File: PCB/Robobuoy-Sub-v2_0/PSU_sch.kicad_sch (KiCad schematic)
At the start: 69 parts, among them J201 Accu 1, J202 LoadbalanceAccu1, J203 LoadbalanceAccu2, J204 CHARGE/ON-OFF, J205 Accu 2, J206 ESCSB, J207 ESCBB, Q201 AO3400A, Q202 AO3400A, Q203 AO3400A, Q204 AO3400A, Q205 AO3400A, Q206 AO3400A, Q207 AO3400A, Q208 AO3400A, SW201 On/Off, U201 TPS5430DDAR, U202 SN74LV1T34DBV, U203 SN74LV1T34DBV, U204 TLV61046ADB

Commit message: Pc programm starting to code
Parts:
- removed C216: 100n, A_Device:C_0603, symbol Device:C_Small
- removed Q203, Q205, Q207: AO3400A, Package_TO_SOT_SMD:SOT-23, symbol Transistor_FET:2N7002
- removed R208: 1.8k, A_Device:R_0603, symbol Device:R_Small
- removed U202: SN74LV1T34DBV, Package_TO_SOT_SMD:SOT-23-5, symbol Logic_LevelTranslator:SN74LV1T34DBV
- added Q203, Q205, Q207, Q209: AO3401A, Package_TO_SOT_SMD:SOT-23, symbol Transistor_FET:AO3401A
- added R208, R214, R215: 10K, A_Device:R_0603, symbol Device:R
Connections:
- net GND: now also J206.1 (Pin_1), R208.1
- net PWR_ESC_SB: now also R209.2
- net Vbatt: now also Q203.2 (S), Q205.2 (S), Q207.2 (S), Q209.2 (S), R215.1; no longer J206.2 (Pin_2)
- net at Q201.1 (G), R209.1: no longer TP207.1
- net at D205.2 (A): now also J206.2 (Pin_2), Q203.3 (D), Q205.3 (D), Q207.3 (D), Q209.3 (D)
- new net: Q201.3 (D), R214.1
- new net: D205.1 (K), R208.2
- new net: Q203.1 (G), Q205.1 (G), Q207.1 (G), Q209.1 (G), R214.2, R215.2, TP207.1
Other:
- moved on the sheet: D205, J206, TP207

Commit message: Many changes again :)
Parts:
- removed C209, C210, C215, C217, C219: 100n, A_Device:C_0603, symbol Device:C_Small
- removed C218: 4.7uF/10V, A_Device:C_1206_(1.6), symbol Device:C_Small
- removed D206: ESC_SB, A_Passive:LED_0805, symbol Device:LED_Small
- removed D6: 5V, A_Passive:LED_0805, symbol Device:LED_Small
- removed J202: LoadbalanceAccu1, Connector_JST:JST_XH_B7B-XH-A_1x07_P2.50mm_Vertical, symbol Connector:Conn_01x07_Pin
- removed J203: LoadbalanceAccu2, Connector_JST:JST_XH_B7B-XH-A_1x07_P2.50mm_Vertical, symbol Connector:Conn_01x07_Pin
- removed J204: CHARGE/ON-OFF, A_Connector:T4140012121000, symbol Connector:Conn_01x12_Socket
- removed L202: 10uH, A_Device:FTC252012S, symbol Device:L_Small
- removed Q204, Q206, Q208: AO3400A, Package_TO_SOT_SMD:SOT-23, symbol Transistor_FET:2N7002
- removed R19, R210: 1.8k, A_Device:R_0603, symbol Device:R_Small
- removed R20: 1k, A_Device:R_0603, symbol Device:R_Small
- removed R211: 100, A_Device:R_0603, symbol Device:R_Small
- removed R212: 82K, A_Device:R_0603, symbol Device:R_Small
- removed R213: 15K, A_Device:R_0603, symbol Device:R_Small
- removed TP208: ESC_BB-POWER-5V, A_Pads_Pins:Testpad_1, symbol Connector:TestPoint_Small
- removed TP209: 0.795V, A_Pads_Pins:Testpad_1, symbol Connector:TestPoint_Small
- removed TP210: 5V, A_Pads_Pins:Testpad_1, symbol Connector:TestPoint_Small
- removed U203: SN74LV1T34DBV, Package_TO_SOT_SMD:SOT-23-5, symbol Logic_LevelTranslator:SN74LV1T34DBV
- removed U204: TLV61046ADB, Package_TO_SOT_SMD:SOT-23-6, symbol Regulator_Switching:TLV61046ADB
- added D203: ESC_BB, A_Passive:LED_0805, symbol Device:LED_Small
- added Q204, Q206, Q208, Q210: AO3401A, Package_TO_SOT_SMD:SOT-23, symbol Transistor_FET:AO3401A
- added R206: 10K, A_Device:R_0603, symbol Device:R_Small
- added R207: 100, A_Device:R_0603, symbol Device:R_Small
- added R210, R211, R212: 10K, A_Device:R_0603, symbol Device:R
- added TP205: ESC_SB-POWER-5V, A_Pads_Pins:Testpad_1, symbol Connector:TestPoint_Small
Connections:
- net +3.3V: now also R206.2
- net GND: now also J207.1 (Pin_1), R212.1
- net PWR_ESC_BB: now also R207.2
- net Vbatt: now also Q204.2 (S), Q206.2 (S), Q208.2 (S), Q210.2 (S), R211.1; no longer J207.2 (Pin_2)
- net at Q202.1 (G): now also R207.1
- net at Q202.3 (D): now also R210.1; no longer J207.1 (Pin_1)
- net at D7.2 (A): now also R206.1
- new net: D203.2 (A), J207.2 (Pin_2), Q204.3 (D), Q206.3 (D), Q208.3 (D), Q210.3 (D)
- new net: D203.1 (K), R212.2
- new net: Q204.1 (G), Q206.1 (G), Q208.1 (G), Q210.1 (G), R210.2, R211.2, TP205.1
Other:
- moved on the sheet: D205, D7, J206, J207, Q201, Q203, Q205, Q207, Q209, R208, R209, R214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

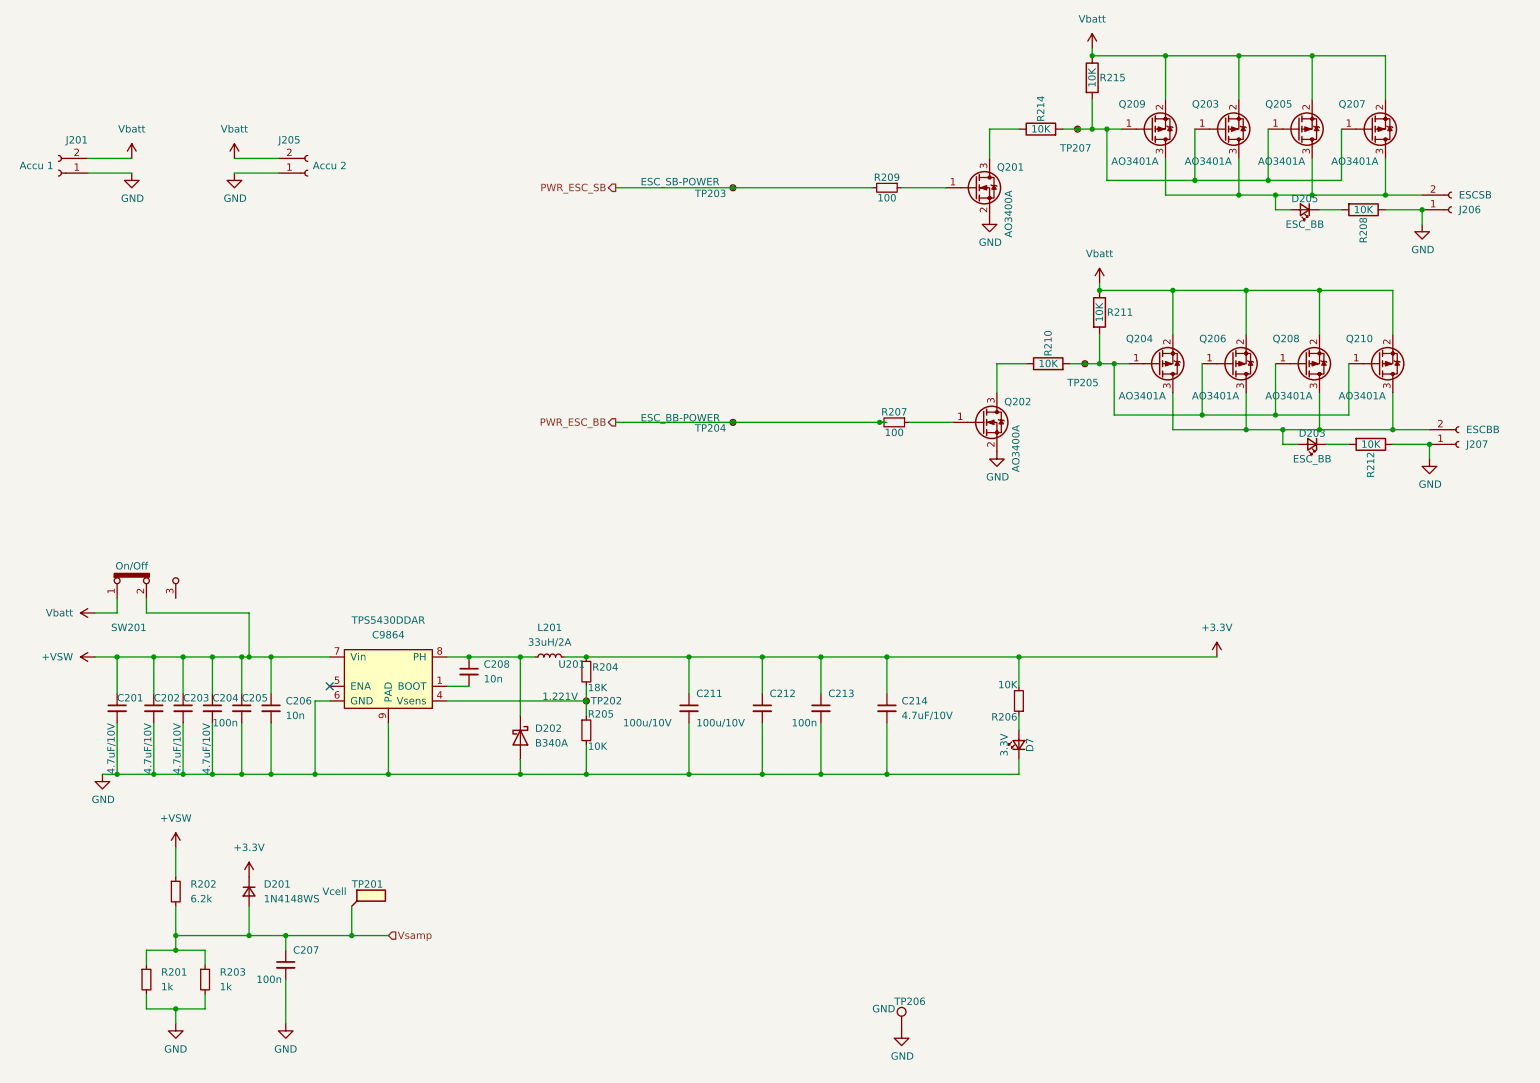
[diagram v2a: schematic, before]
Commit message: Struct re defined. not finished yet
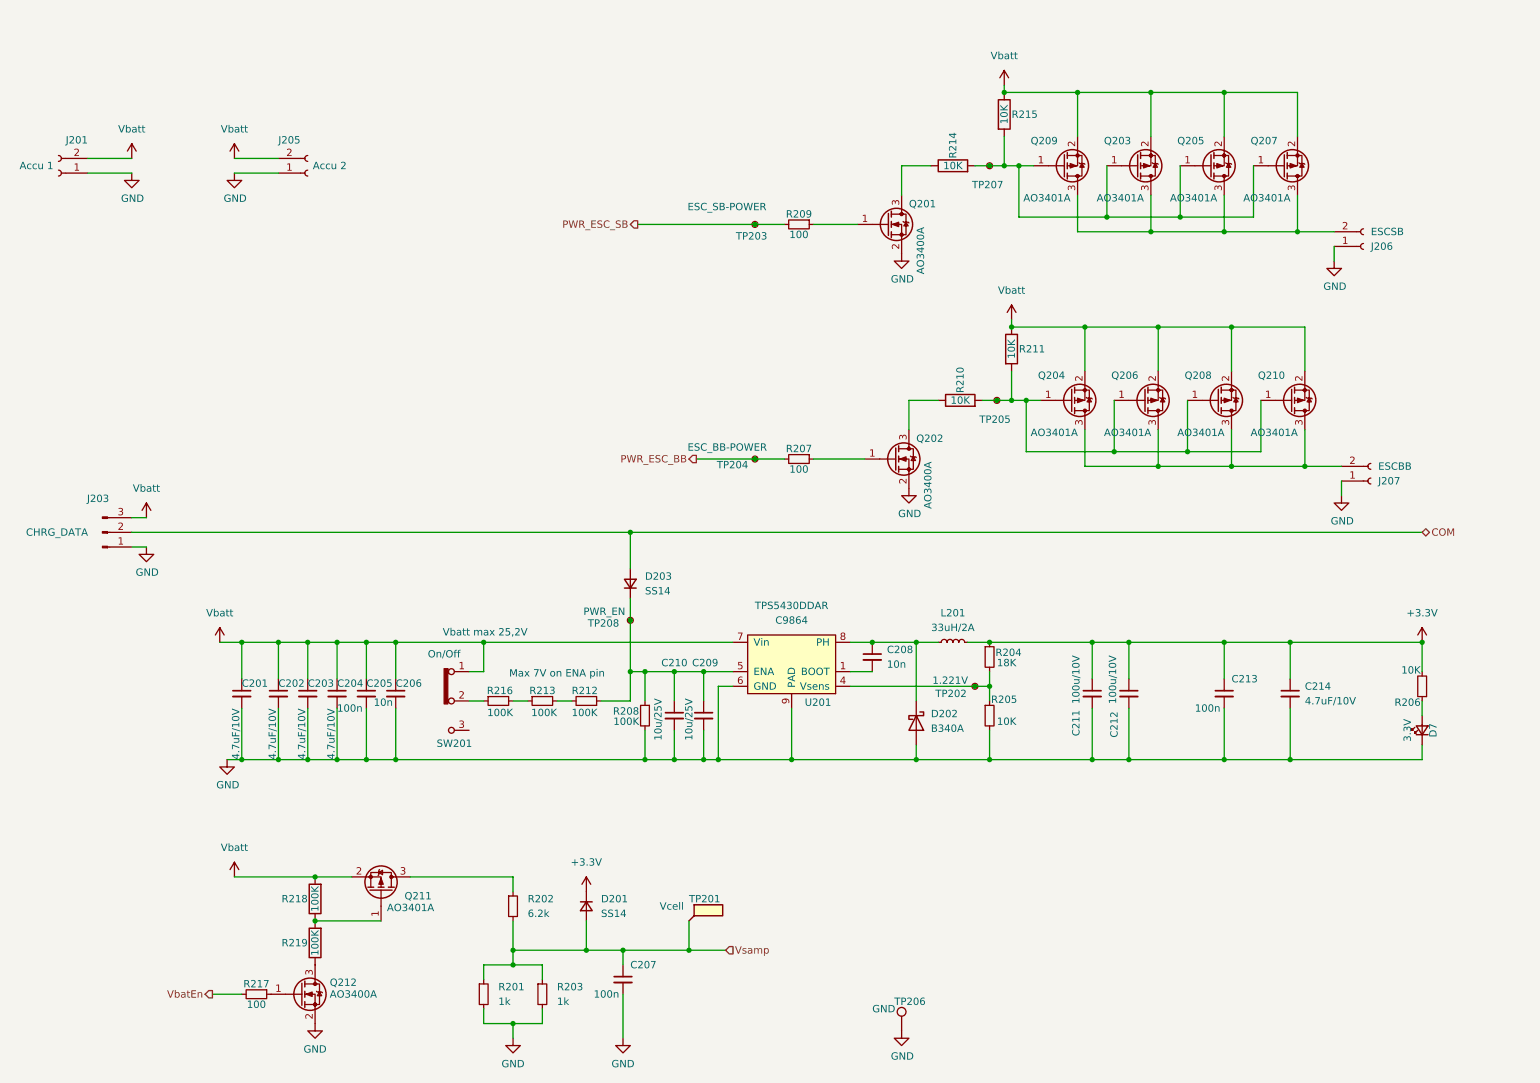
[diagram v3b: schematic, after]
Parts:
- removed D203, D205: ESC_BB, A_Passive:LED_0805, symbol Device:LED_Small
- removed R208, R212: 10K, A_Device:R_0603, symbol Device:R
- added C209, C210: 10u/25V, A_Device:C_0805, symbol Device:C_Small
- added D203: SS14, A_Device:D_SMA_4.3x3x2.4, symbol Device:D_Small
- added J203: CHRG_DATA, Connector_JST:JST_XH_B3B-XH-A_1x03_P2.50mm_Vertical, symbol Connector:Conn_01x03_Pin
- added Q211: AO3401A, Package_TO_SOT_SMD:SOT-23, symbol Transistor_FET:AO3401A
- added Q212: AO3400A, Package_TO_SOT_SMD:SOT-23, symbol Transistor_FET:2N7002
- added R208, R212, R213, R216: 100K, A_Device:R_0603, symbol Device:R_Small
- added R217: 100, A_Device:R_0603, symbol Device:R_Small
- added R218, R219: 100K, A_Device:R_0603, symbol Device:R
- added TP208: PWR_EN, A_Pads_Pins:Testpad_1, symbol Connector:TestPoint_Small
- D201: value 1N4148WS -> SS14; footprint A_Device:D_SOD-323_1.8x1.4x1.15 -> A_Device:D_SMA_4.3x3x2.4; LCSC C2128 -> C2480
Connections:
- net GND: now also C209.2, C210.2, J203.1 (Pin_1), Q212.2 (S), R208.2
- net Vbatt: now also C201.1, C202.1, C203.1, C204.1, C205.1, C206.1, U201.7 (Vin), J203.3 (Pin_3), Q211.2 (S), R218.2
- net at U201.5 (ENA): now also C209.1, C210.1, D203.1 (K), R208.1, R212.1, TP208.1
- removed net +VSW: C201.1, C202.1, C203.1, C204.1, C205.1, C206.1, R202.1, SW201.2, U201.7 (Vin)
- new net: Q212.1 (G), R217.1
- new net: Q212.3 (D), R219.1
- new net: R216.1, SW201.2
- new net: R213.1, R216.2
- new net: Q211.3 (D), R202.1
- new net: R212.2, R213.2
- new net: Q211.1 (G), R218.1, R219.2
- new net COM: D203.2 (A), J203.2 (Pin_2)
- new net VbatEn: R217.2
- no-connect marks 1 -> 0
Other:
- note added: "Max 7V on ENA pin"
- note added: "Vbatt max 25,2V"
- moved on the sheet: C201, C202, C203, C204, C205, C206, C207, C208, C211, C212, C213, C214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

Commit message: Many changes
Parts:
- removed J201: Accu 1, A_Connector:AMASS_XT60-M_1x02_P7.20mm_Vertical, symbol Connector:Conn_01x02_Socket
- removed J203: CHRG_DATA, Connector_JST:JST_XH_B3B-XH-A_1x03_P2.50mm_Vertical, symbol Connector:Conn_01x03_Pin
- removed J205: Accu 2, A_Connector:AMASS_XT60-M_1x02_P7.20mm_Vertical, symbol Connector:Conn_01x02_Socket
- removed J206: ESCSB, A_Connector:AMASS_XT60-F_1x02_P7.20mm_Vertical, symbol Connector:Conn_01x02_Socket
- removed J207: ESCBB, A_Connector:AMASS_XT60-F_1x02_P7.20mm_Vertical, symbol Connector:Conn_01x02_Socket
- removed Q201, Q202: AO3400A, Package_TO_SOT_SMD:SOT-23, symbol Transistor_FET:2N7002
- removed Q203, Q204, Q205, Q206, Q207, Q208, Q209, Q210: AO3401A, Package_TO_SOT_SMD:SOT-23, symbol Transistor_FET:AO3401A
- removed R207, R209: 100, A_Device:R_0603, symbol Device:R_Small
- removed R210, R211, R214, R215: 10K, A_Device:R_0603, symbol Device:R
- removed TP203: ESC_SB-POWER, A_Pads_Pins:Testpad_1, symbol Connector:TestPoint_Small
- removed TP204: ESC_BB-POWER, A_Pads_Pins:Testpad_1, symbol Connector:TestPoint_Small
- removed TP205, TP207: ESC_SB-POWER-5V, A_Pads_Pins:Testpad_1, symbol Connector:TestPoint_Small
- added D201: SS14, A_Device:D_SMA_4.3x3x2.4, symbol Device:D_Small
- added J202: CHRG/DATA, Connector_Wire:SolderWire-0.75sqmm_1x03_P4.8mm_D1.25mm_OD2.3mm, symbol Connector:Conn_01x03_Pin
- D204: renamed from D202; value B340A -> SS54; LCSC C85098 -> C22452
- renumbered C210 to C208, C208 to C210, D201 to D202, Q212 to Q201, Q211 to Q202, R217 to R201, R218 to R202, R219 to R203, R201 to R204, R216 to R205, R202 to R206, R213 to R207, R203 to R208, R212 to R209, R208 to R210, R204 to R211, R205 to R212, R206 to R213, TP208 to TP201, TP201 to TP202, TP206 to TP203, TP202 to TP204
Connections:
- net COM: now also J202.2 (Pin_2)
- net GND: now also J202.1 (Pin_1)
- net Vbatt: now also J202.3 (Pin_3)
- net at C208.1, C209.1, D203.1 (K)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: now also D201.1 (K)
- new net PwrEn: D201.2 (A)
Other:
- moved on the sheet: D203

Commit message: Pcb changes
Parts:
- removed C201, C202, C203: 4.7uF/10V, A_Device:C_1206_(1.6), symbol Device:C_Small
- removed J202: CHRG/DATA, Connector_Wire:SolderWire-0.75sqmm_1x03_P4.8mm_D1.25mm_OD2.3mm, symbol Connector:Conn_01x03_Pin
- added J201: AccuSB, Connector_Wire:SolderWire-0.75sqmm_1x03_P4.8mm_D1.25mm_OD2.3mm, symbol Connector:Conn_01x03_Socket
- added J202: AccuBB, Connector_Wire:SolderWire-0.75sqmm_1x03_P4.8mm_D1.25mm_OD2.3mm, symbol Connector:Conn_01x03_Socket
- added J205: CHRG/DATA, Connector_Wire:SolderWire-0.75sqmm_1x03_P4.8mm_D1.25mm_OD2.3mm, symbol Connector:Conn_01x03_Socket
- D201, D202, D203: value SS14 -> SM4007PL; footprint A_Device:D_SMA_4.3x3x2.4 -> A_Device:D_SOD-123_2.85x1.8x1.3; LCSC C2480 -> C64898
- renumbered C204 to C201, C205 to C202, C206 to C203, C207 to C204, C208 to C205, C209 to C206, C210 to C207, C211 to C208, C212 to C209, C213 to C210, C214 to C211, D7 to D205
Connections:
- net COM: now also J205.3 (Pin_3)
- net GND: now also J201.2 (Pin_2), J201.3 (Pin_3), J202.2 (Pin_2), J202.3 (Pin_3), J205.1 (Pin_1)
- net Vbatt: now also J201.1 (Pin_1), J202.1 (Pin_1), J205.2 (Pin_2)
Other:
- moved on the sheet: C201, C202
